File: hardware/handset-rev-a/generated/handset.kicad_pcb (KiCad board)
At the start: 4 copper layers, 66 x 142 mm, 281 parts, among them J1 2053380002, J10 LF_COIL_TUNING_REQUIRED, J16 EXPANSION_J16, J2 PACK_NTC_10K_B3435, J20 LORA_915_ANT, J21 CC1101_915_ANT, J22 GNSS_PASSIVE_ANT, J23 DM3D-SF, J24 TSAL6400_CASE_LED, J25 TSOP38438_CASE_RX, J26 FH12A-50S-0.5SH(55), J3 MEDIA_SPEAKER_DIFFERENTIAL, J4 CALL_AUDIO_FROM_MODEM_ADAPTER, J5 CALL_EARPIECE, J6 CALL_MIC, J7 PIM447_HARNESS_VERIFY, J8 MODEM_ADAPTER_3V3_LOGIC, J9 MODEM_POWER_ADAPTER_REQUIRED, Q1 AO3400A, Q3 AO3400A, Q4 AO3400A, Q5 AO3400A, Q6 AO3401A, Q7 AO3400A, Q8 AO3400A, SW1 1, SW10 10, SW11 11, SW12 12, SW13 13, SW14 14, SW15 15, SW16 16, SW17 MCU_BOOT, SW18 MCU_EN, SW19 POWER, SW2 2, SW3 3, SW4 4, SW5 5, SW6 6, SW7 7, SW8 8, SW9 9, U1 ESP32-S3-WROOM-1-N16R8, U10 TPS61023DRLR, U11 TPS62840DLCR, U12 MAX-M10S-00B-01, U13 ST25R3916B-AQET, U14 TPS2553DBVR, U15 TPD4E05U06DQAR, U16 TPD4E05U06DQAR, U17 TPD4E05U06DQAR, U18 SN74AHCT125PWR, U19 SN74LVC1G17DBVR, U2 TCA8418RTWR, U20 TPS63070RNMR, U21 TPS25200DRVR, U22 TUSB320LAIRWBR, U23 TLV70433DBVR, U24 TCA9536DGKR, U25 STM32G031G8U6, U26 TPS7A0230PDBVR, U27 TCA9800DGKR, U28 TPS7A2030PDBVR, U29 SN74LVC244APWR, U3 BQ25186DLHR, U30 SN74LVC2G125DCUR, U31 TCA9406DCUR, U32 CAT4004AHU2-GT3, U33 TCA9537DGSR, U34 SN74CB3Q3245PWR, U35 SN74HCS10PWR, U36 0900FM15K0039001E, U37 BGS12WN6E6327, U4 SX1262IMLTRT, U5 CC1101RGPR, U6 MAX98357AETE+, U7 TPS63802DLAR, U8 MAX17048G+T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

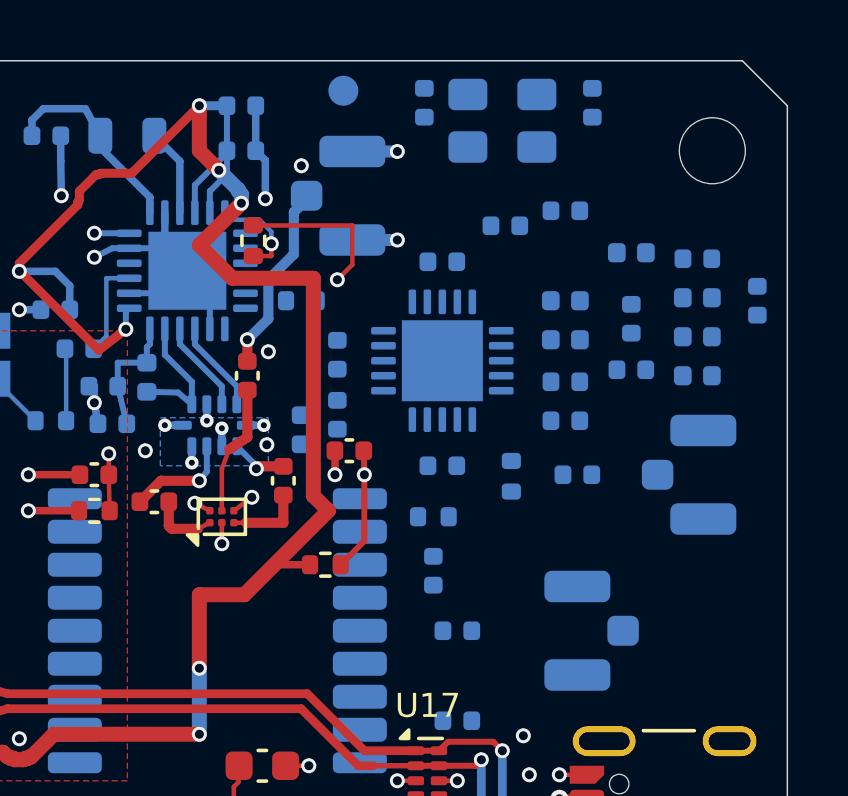
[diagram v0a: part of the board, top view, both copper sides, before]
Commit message: feat: route CC1101 clock and local supplies
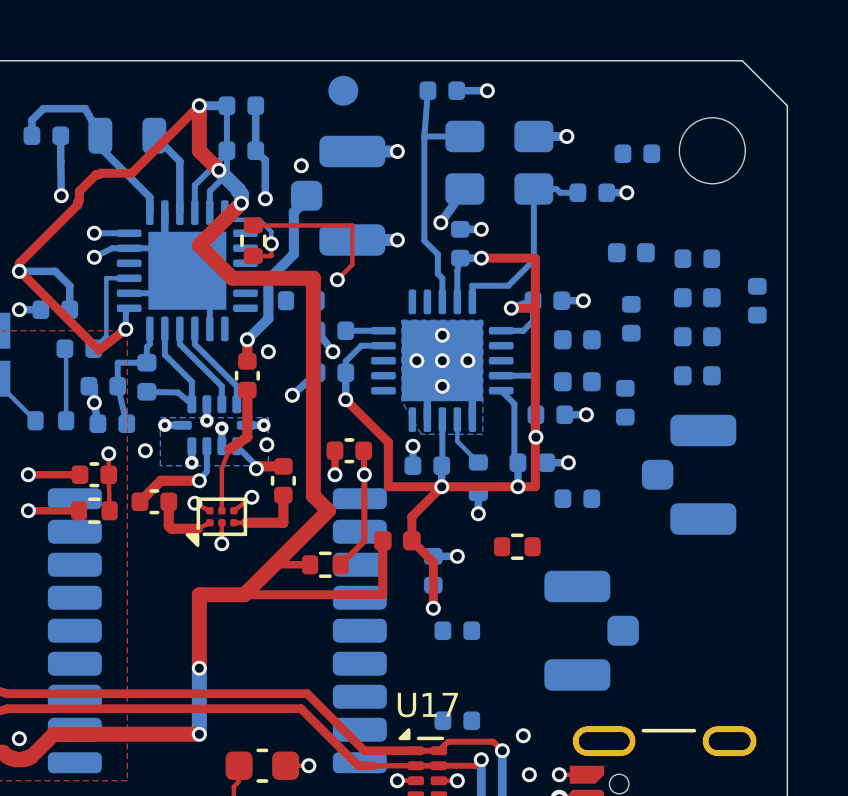
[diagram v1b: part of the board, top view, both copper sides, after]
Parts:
- L11, R12: moved to F.Cu
- U5: footprint Package_DFN_QFN:Texas_RGP0020D_VQFN-20-1EP_4x4mm_P0.5mm_EP2.7x2.7mm -> Handset:CC1101_RGP20_MaskedThermalVias
- moved L11 4.89 mm to (120.0, 45.0), turned to 0 degrees
- moved C66 3.06 mm to (128.0, 32.1)
- moved C62 3.00 mm to (126.5, 33.4), turned to 0 degrees
- moved R12 2.97 mm to (124.0, 45.2)
- moved C70 2.87 mm to (125.0, 37.0)
- moved C72 1.78 mm to (124.5, 42.4)
- moved L6 1.46 mm to (126.0, 39.7)
- moved C12 1.41 mm to (117.8, 39.4), turned to 180 degrees
- moved Y2 1.40 mm to (123.4, 32.4)
- moved L5 1.36 mm to (126.0, 38.3)
- moved C71 1.21 mm to (125.1, 40.8)
- moved C68 1.12 mm to (127.6, 40.4), turned to 90 degrees
- moved R11 1.10 mm to (122.7, 42.9), turned to -90 degrees
- moved C69 0.85 mm to (122.1, 35.1), turned to 90 degrees
- moved C11 0.82 mm to (117.8, 38.0), turned to 180 degrees
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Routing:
- net CC_VDD: track 0.00 -> 40.6 mm, vias 0 -> 7
- net GND: track 424.6 -> 439.7 mm, vias 193 -> 211
- net CC_X1: track 0.00 -> 8.64 mm
- net CC_X2: track 0.00 -> 6.84 mm
- net +3V3: track 503.2 -> 509.6 mm
- net CC_RBIAS: track 0.00 -> 1.72 mm
- net CC_DCOUPL: track 0.00 -> 1.26 mm

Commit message: feat: route CC1101 matching and antenna path
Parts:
- moved C65 4.31 mm to (131.7, 41.3), turned to 0 degrees
- moved L10 3.41 mm to (130.3, 40.3), turned to 180 degrees
- moved C66 2.81 mm to (128.2, 34.9)
- moved C64 2.15 mm to (129.0, 37.5)
- moved J21 1.92 mm to (130.5, 44.7)
- moved C63 1.44 mm to (127.5, 39.0), turned to -90 degrees
- moved L8 1.28 mm to (129.0, 39.0)
- moved L7 1.24 mm to (127.0, 36.4), turned to 90 degrees
- moved L9 1.17 mm to (131.0, 38.9)
- moved C67 0.98 mm to (126.9, 43.2), turned to -90 degrees
- moved C68 0.61 mm to (127.5, 41.0), turned to 0 degrees
- moved L6 0.40 mm to (126.0, 39.3)
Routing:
- net GND: track 439.7 -> 445.0 mm, vias 211 -> 220
- net CC_BAL_P: track 0.00 -> 4.53 mm
- net CC_DC_BLOCK: track 0.00 -> 4.32 mm
- net CC_LPF: track 0.00 -> 4.29 mm
- net CC_BAL_N: track 0.00 -> 4.10 mm
- net CC_MATCH: track 0.00 -> 2.53 mm
- net CC_RF_50R: track 0.00 -> 2.51 mm
- net CC_RF_N: track 0.00 -> 2.18 mm
- net CC_RF_P: track 0.00 -> 2.14 mm
- net CC_SHUNT: track 0.00 -> 1.69 mm

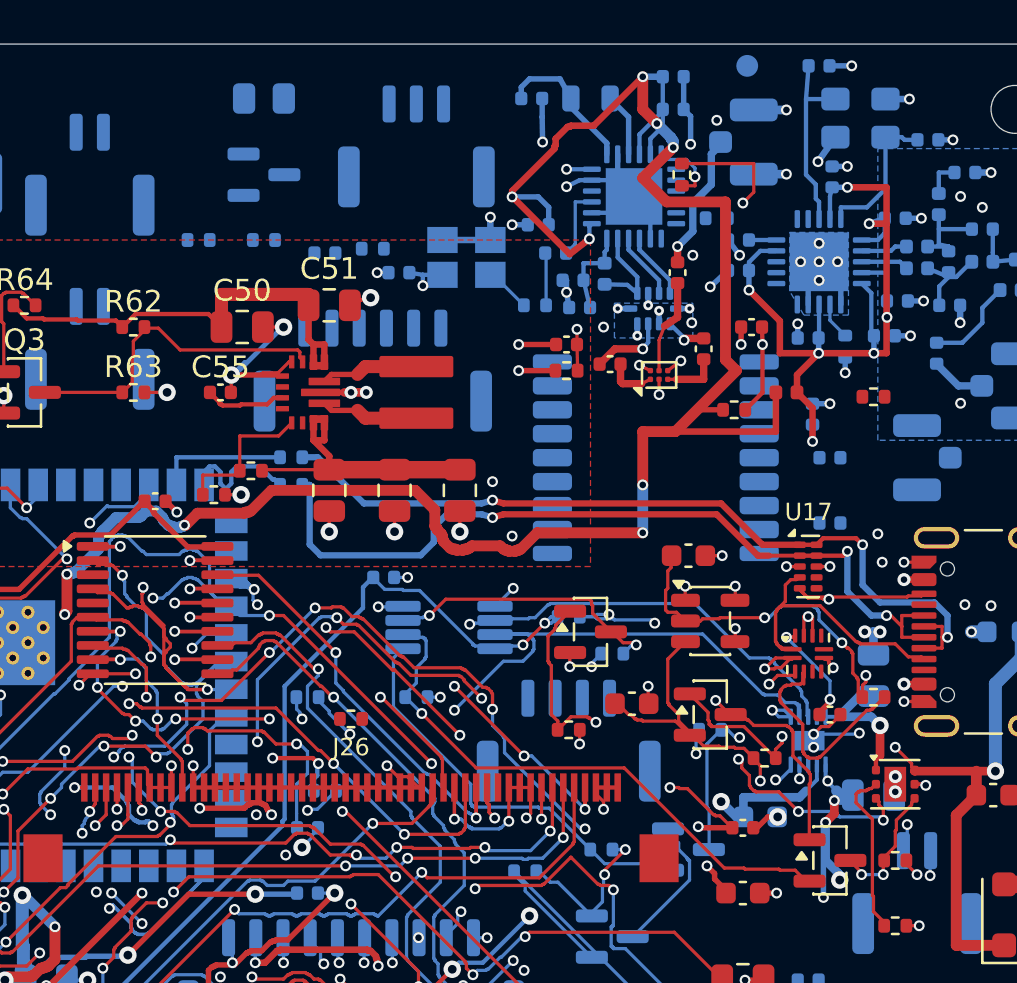
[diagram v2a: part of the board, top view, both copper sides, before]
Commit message: feat: route CC1101 digital interface
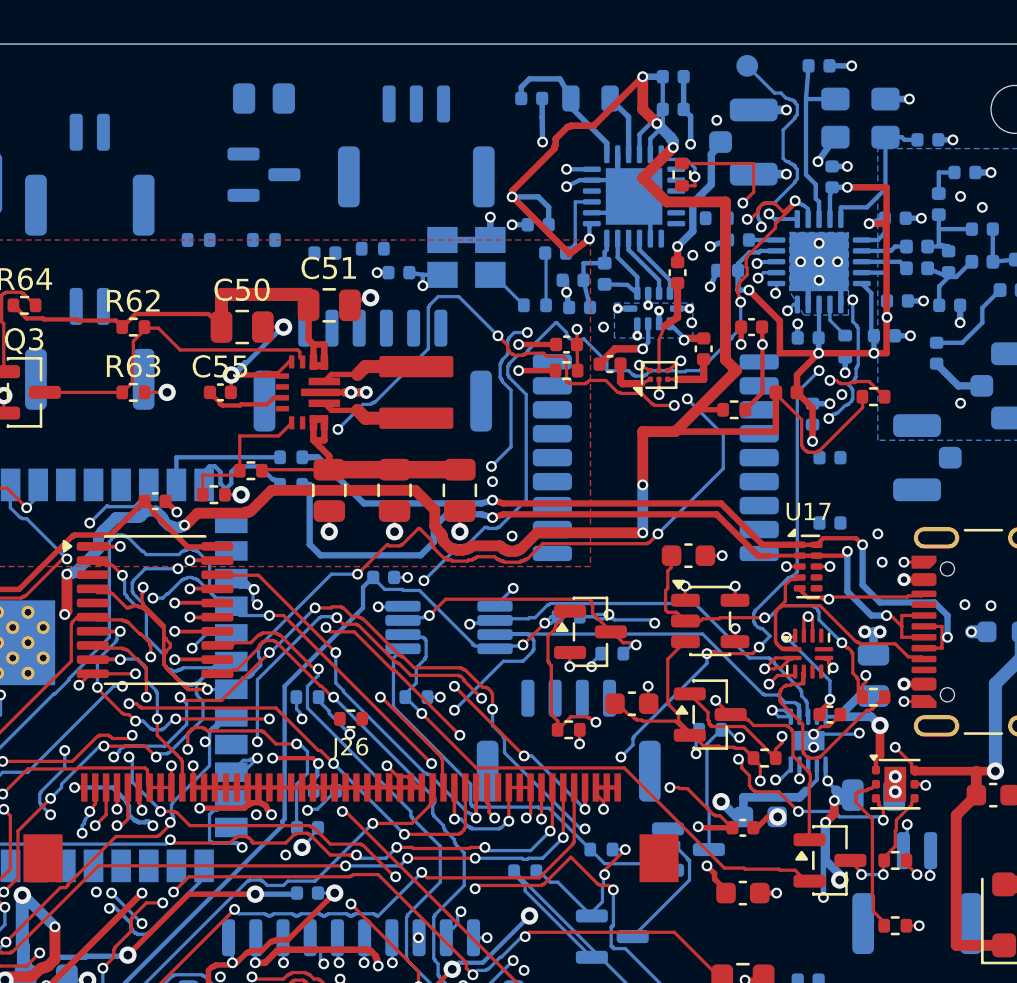
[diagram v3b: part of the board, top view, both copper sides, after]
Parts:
- moved C12 0.50 mm to (117.3, 39.4)
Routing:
- net CC_GDO0: track 0.00 -> 70.6 mm, vias 0 -> 6
- net CC_CS: track 0.00 -> 66.9 mm, vias 0 -> 6
- net SPI_SCK: track 70.8 -> 131.2 mm, vias 8 -> 15
- net SPI_MISO: track 59.8 -> 113.7 mm, vias 9 -> 14
- net SPI_MOSI: track 79.6 -> 120.2 mm, vias 7 -> 11
- net CC_GDO2: track 0.00 -> 14.3 mm, vias 0 -> 2
- net +3V3: track 509.6 -> 516.9 mm
- net I2C_SCL: track 170.7 -> 176.8 mm
- net CC_VDD: track 40.6 -> 41.5 mm
